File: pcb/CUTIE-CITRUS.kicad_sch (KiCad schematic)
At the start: 0 parts

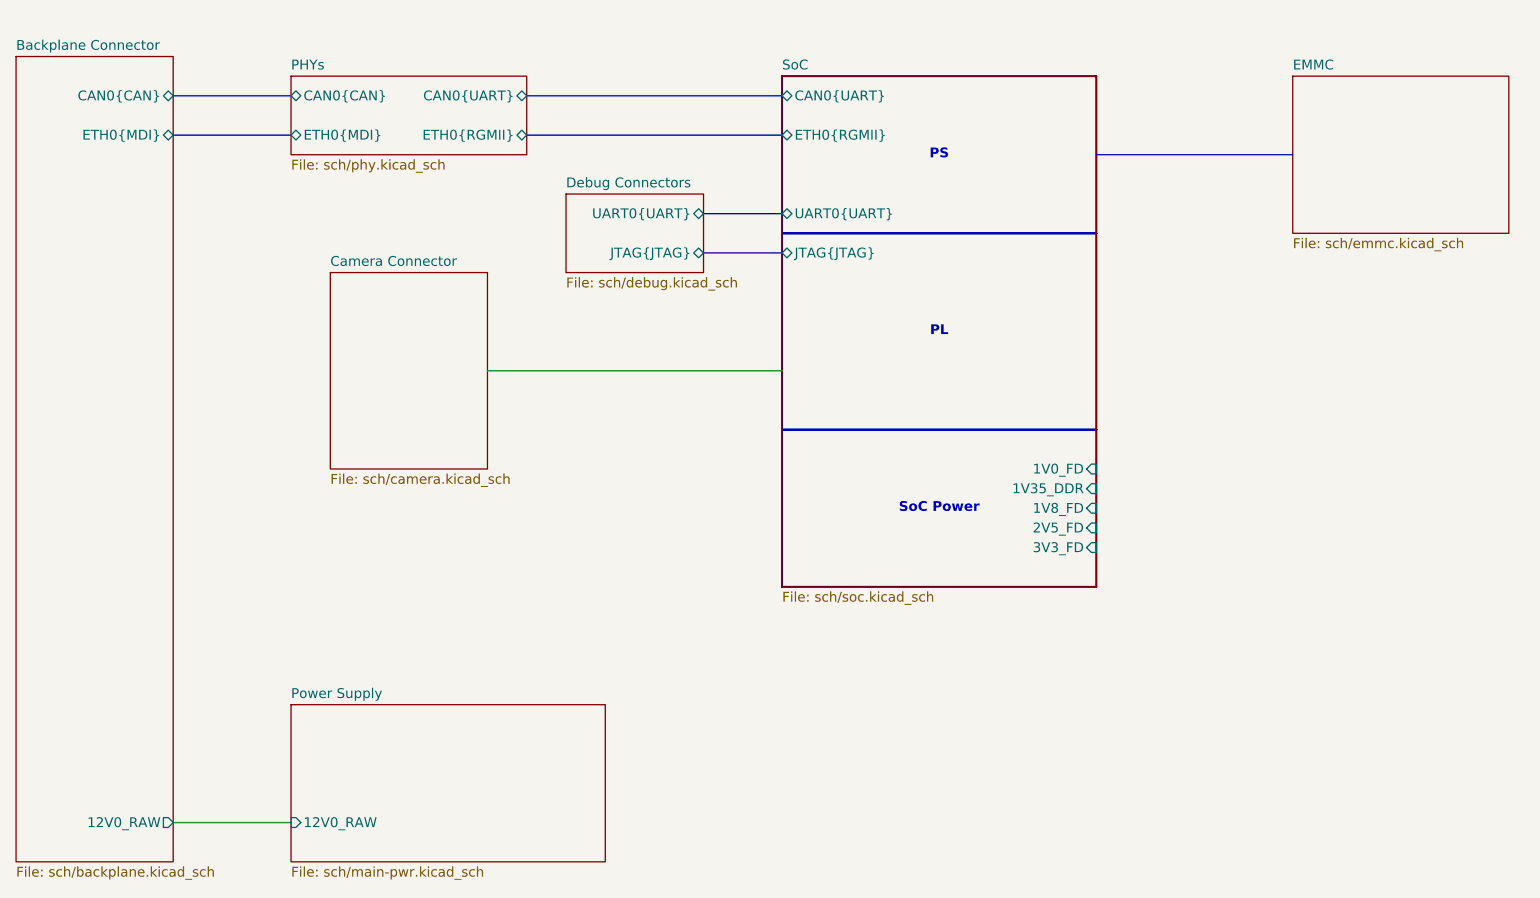
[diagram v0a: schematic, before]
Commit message: byte swapping and rough layout
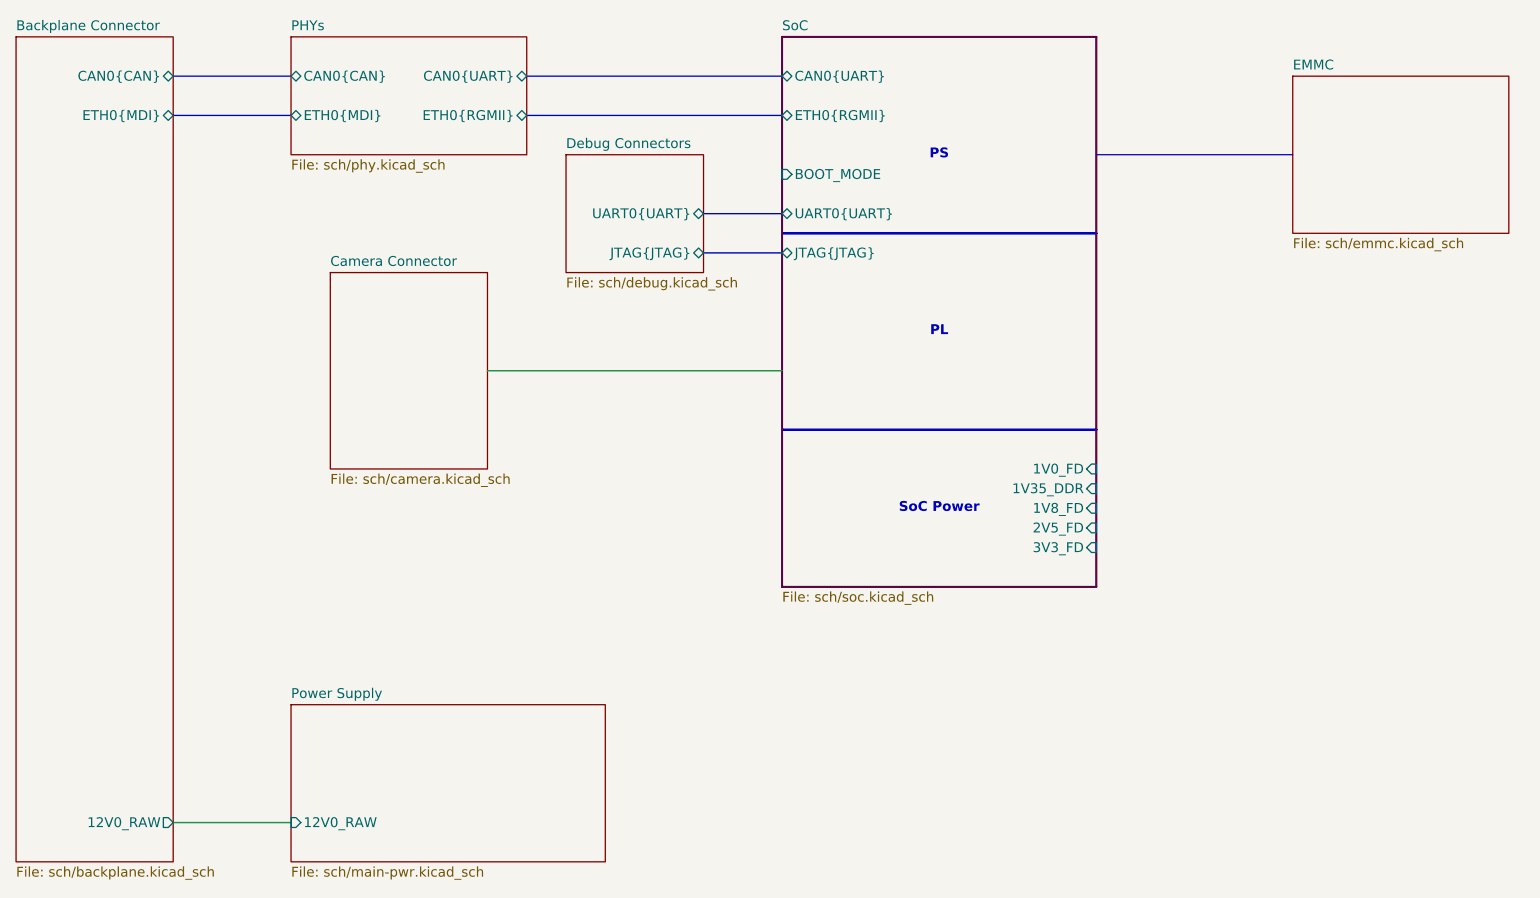
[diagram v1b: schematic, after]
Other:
- sheet SoC ports: added BOOT_MODE; removed none
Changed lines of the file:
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@@
 	)
 	(rectangle
-		(start 157.48 50.8)
+		(start 157.48 45.72)
 		(end 198.12 71.12)
 		(stroke
@@
 	(bus
 		(pts
-			(xy 78.74 53.34) (xy 93.98 53.34)
+			(xy 78.74 50.8) (xy 93.98 50.8)
 		)
 		(stroke
@@
 	(bus
 		(pts
-			(xy 124.46 58.42) (xy 157.48 58.42)
-		)
-		(stroke
-			(width 0)
-			(type default)
-		)
-	)
-	(bus
-		(pts
-			(xy 124.46 53.34) (xy 157.48 53.34)
+			(xy 124.46 55.88) (xy 157.48 55.88)
+		)
+		(stroke
+			(width 0)
+			(type default)
+		)
+	)
+	(bus
+		(pts
+			(xy 124.46 50.8) (xy 157.48 50.8)
 		)
 		(stroke
@@
 	(bus
 		(pts
-			(xy 78.74 58.42) (xy 93.98 58.42)
+			(xy 78.74 55.88) (xy 93.98 55.88)
 		)
 		(stroke
@@
 	)
 	(sheet
-		(at 129.54 66.04)
-		(size 17.78 10.16)
+		(at 129.54 60.96)
+		(size 17.78 15.24)
 		(exclude_from_sim no)
 		(in_bom yes)
@@
 		)
 		(property "Sheetname" "Debug Connectors"
-			(at 129.54 65.3284 0)
+			(at 129.54 60.2484 0)
 			(show_name no)
 			(do_not_autoplace no)
@@
 	)
 	(sheet
-		(at 58.42 48.26)
-		(size 20.32 104.14)
+		(at 58.42 45.72)
+		(size 20.32 106.68)
 		(exclude_from_sim no)
 		(in_bom yes)
@@
 		)
 		(property "Sheetname" "Backplane Connector"
-			(at 58.42 47.5484 0)
+			(at 58.42 45.0084 0)
 			(show_name no)
 			(do_not_autoplace no)
@@
 		)
 		(pin "CAN0{CAN}" bidirectional
-			(at 78.74 53.34 0)
+			(at 78.74 50.8 0)
 			(effects
 				(font
@@
 		)
 		(pin "ETH0{MDI}" bidirectional
-			(at 78.74 58.42 0)
+			(at 78.74 55.88 0)
 			(effects
 				(font
@@
 	)
 	(sheet
-		(at 93.98 50.8)
-		(size 30.48 10.16)
+		(at 93.98 45.72)
+		(size 30.48 15.24)
 		(exclude_from_sim no)
 		(in_bom yes)
@@
 		)
 		(property "Sheetname" "PHYs"
-			(at 93.98 50.0884 0)
+			(at 93.98 45.0084 0)
 			(show_name no)
 			(do_not_autoplace no)
@@
 		)
 		(pin "CAN0{CAN}" bidirectional
-			(at 93.98 53.34 180)
+			(at 93.98 50.8 180)
 			(effects
 				(font
@@
 		)
 		(pin "ETH0{RGMII}" bidirectional
-			(at 124.46 58.42 0)
+			(at 124.46 55.88 0)
 			(effects
 				(font
@@
 		)
 		(pin "CAN0{UART}" bidirectional
-			(at 124.46 53.34 0)
+			(at 124.46 50.8 0)
 			(effects
 				(font
@@
 		)
 		(pin "ETH0{MDI}" bidirectional
-			(at 93.98 58.42 180)
+			(at 93.98 55.88 180)
 			(effects
 				(font
@@
 	)
 	(sheet
-		(at 157.48 50.8)
-		(size 40.64 66.04)
+		(at 157.48 45.72)
+		(size 40.64 71.12)
 		(exclude_from_sim no)
 		(in_bom yes)
@@
 		)
 		(property "Sheetname" "SoC"
-			(at 157.48 50.0884 0)
+			(at 157.48 45.0084 0)
 			(show_name no)
 			(do_not_autoplace no)
@@
 		)
 		(pin "ETH0{RGMII}" bidirectional
-			(at 157.48 58.42 180)
+			(at 157.48 55.88 180)
 			(effects
 				(font
@@
 		)
 		(pin "CAN0{UART}" bidirectional
-			(at 157.48 53.34 180)
+			(at 157.48 50.8 180)
 			(effects
 				(font
@@
 			)
 		)
+		(pin "BOOT_MODE" input
+			(at 157.48 63.5 180)
+			(effects
+				(font
+					(size 1.27 1.27)
+				)
+				(justify left)
+			)
+		)

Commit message: power
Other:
- sheet Backplane Connector ports: added VBUS; removed 12V0_RAW
- sheet Power Supply ports: added VBUS; removed 12V0_RAW
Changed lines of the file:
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@@
-	(wire
-		(pts
-			(xy 78.74 147.32) (xy 93.98 147.32)
-		)
-		(stroke
-			(width 0)
-			(type default)
-		)
-	)
 	(wire
 		(pts
@@
 			)
 		)
-		(pin "12V0_RAW" output
-			(at 78.74 147.32 0)
+		(pin "VBUS" output
+			(at 78.74 142.24 0)
 			(effects
 				(font
@@
 			)
 		)
-		(pin "12V0_RAW" input
-			(at 93.98 147.32 180)
-			(effects
-				(font
+		(pin "VBUS" input
+			(at 93.98 142.24 180)
+			(effects
+				(font
